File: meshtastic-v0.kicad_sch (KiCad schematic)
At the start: 0 parts

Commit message: Connect VSYS/3V3 sheet pins, sync R22, document remaining ERC state
Schematic/PCB edits: wire up the dangling VSYS and 3V3 hierarchical
sheet pins on the root sheet, and re-sync the board so R22 reads 1k
on both sides.

ERC 8 -> 6 errors; schematic parity 3 -> 2 issues; DRC still 0
violations and 0 unconnected pads.

README: explain each of the 6 remaining ERC errors (all PWR_FLAG /
no-connect annotations or the intentional JP3/JP4 jumper routing,
none of them wiring defects), and add an assembly note that JP3/JP4
ship unbridged and must be bridged for the display to receive power.

Co-Authored-By: Claude Opus 5 <noreply@anthropic.com>
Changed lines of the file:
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@@
+	(wire
+		(pts
+			(xy 191.77 81.28) (xy 191.77 69.85)
+		)
+		(stroke
+			(width 0)
+			(type default)
+		)
+	)
 	(wire
 		(pts
@@
 	(wire
 		(pts
+			(xy 186.69 69.85) (xy 186.69 78.74)
+		)
+		(stroke
+			(width 0)
+			(type default)
+		)
+	)
+	(wire
+		(pts
 			(xy 269.24 177.8) (xy 269.24 127)
 		)
@@
 	(wire
 		(pts
+			(xy 184.15 81.28) (xy 191.77 81.28)
+		)
+		(stroke
+			(width 0)
+			(type default)
+		)
+	)
+	(wire
+		(pts
 			(xy 189.23 220.98) (xy 189.23 205.74)
 		)
@@
 	(wire
 		(pts
+			(xy 186.69 78.74) (xy 184.15 78.74)
+		)
+		(stroke
+			(width 0)
+			(type default)
+		)
+	)
+	(wire
+		(pts
 			(xy 184.15 205.74) (xy 189.23 205.74)
 		)
@@
 		)
 	)
+	(symbol
+		(lib_id "power:+3V3")
+		(at 191.77 69.85 0)
+		(unit 1)
+		(body_style 1)
+		(exclude_from_sim no)
+		(in_bom yes)
+		(on_board yes)
+		(in_pos_files yes)
+		(dnp no)
+		(fields_autoplaced yes)
+		(property "Reference" "#PWR065"
+			(at 191.77 73.66 0)
+			(hide yes)
+			(show_name no)
+			(do_not_autoplace no)
+			(effects
+				(font
+					(size 1.27 1.27)
+				)
+			)
+		)
+		(property "Value" "+3V3"
+			(at 191.77 64.77 0)
+			(show_name no)
+			(do_not_autoplace no)
+			(effects
+				(font
+					(size 1.27 1.27)
+				)
+			)
+		)
+		(property "Footprint" ""
+			(at 191.77 69.85 0)
+			(hide yes)
+			(show_name no)
+			(do_not_autoplace no)
+			(effects
+				(font
+					(size 1.27 1.27)
+				)
+			)
+		)
+		(property "Datasheet" ""
+			(at 191.77 69.85 0)
+			(hide yes)
+			(show_name no)
+			(do_not_autoplace no)
+			(effects
+				(font
+					(size 1.27 1.27)
+				)
+			)
+		)
+		(property "Description" "Power symbol creates a global label with name \"+3V3\""
+			(at 191.77 69.85 0)
+			(hide yes)
+			(show_name no)
+			(do_not_autoplace no)
+			(effects
+				(font
+					(size 1.27 1.27)
+				)
+			)
+		)
+		(pin "1"
+		)
+		(instances
+			(project "meshtastic-v0"
+				(path "/e4d6fcd6-7415-4955-88fd-f0e430797514"
+					(reference "#PWR065")
+					(unit 1)
+				)
+			)
+		)
+	)
+	(symbol
+		(lib_id "power:VSS")
+		(at 186.69 69.85 0)
+		(unit 1)
+		(body_style 1)
+		(exclude_from_sim no)
+		(in_bom yes)
+		(on_board yes)
+		(in_pos_files yes)
+		(dnp no)
+		(fields_autoplaced yes)
+		(property "Reference" "#PWR012"
+			(at 186.69 73.66 0)
+			(hide yes)
+			(show_name no)
+			(do_not_autoplace no)
+			(effects
+				(font
+					(size 1.27 1.27)
+				)
+			)
+		)
+		(property "Value" "VSYS"
+			(at 186.69 64.77 0)
+			(show_name no)
+			(do_not_autoplace no)
+			(effects
+				(font
+					(size 1.27 1.27)
+				)
+			)
+		)
+		(property "Footprint" ""
+			(at 186.69 69.85 0)
+			(hide yes)
+			(show_name no)
+			(do_not_autoplace no)
+			(effects
+				(font
+					(size 1.27 1.27)
+				)
+			)
+		)
+		(property "Datasheet" ""
+			(at 186.69 69.85 0)
+			(hide yes)
+			(show_name no)
+			(do_not_autoplace no)
+			(effects
+				(font
+					(size 1.27 1.27)
+				)
+			)
+		)
+		(property "Description" "Power symbol creates a global label with name \"VSS\""
+			(at 186.69 69.85 0)
+			(hide yes)
+			(show_name no)
+			(do_not_autoplace no)
+			(effects
+				(font
+					(size 1.27 1.27)
+				)
+			)
+		)
+		(pin "1"
+		)
+		(instances
+			(project "meshtastic-v0"
+				(path "/e4d6fcd6-7415-4955-88fd-f0e430797514"
+					(reference "#PWR012")
+					(unit 1)
+				)
+			)
+		)
+	)

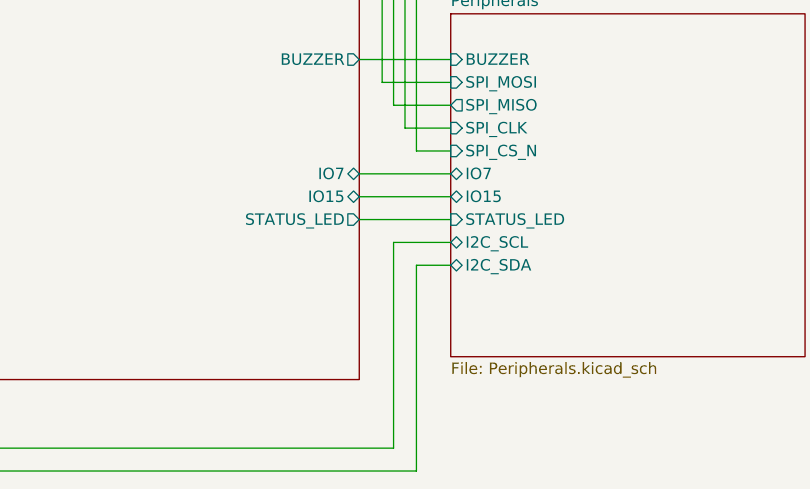
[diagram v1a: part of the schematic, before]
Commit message: Round board corners, re-annotate test points, rewrite README for GitHub
Board: 1.0 mm radius corners; outline now 71.00 x 46.00 mm.
Schematic: test points re-annotated to signal names (SDA1, SLC1,
CSN1, CLK1, MOSI1, MISO1, VS1, G1, G2, IO7, IO15, IO47, RST1, BOOT1).

README rewritten as a GitHub landing page: explains what the board is
for, adds Mermaid system-architecture and power-path diagrams, a
verified pin map traced from the netlist, board specs, and fab
instructions. Drops the ERC/DRC status and issue-tracking sections.

Co-Authored-By: Claude Opus 5 <noreply@anthropic.com>
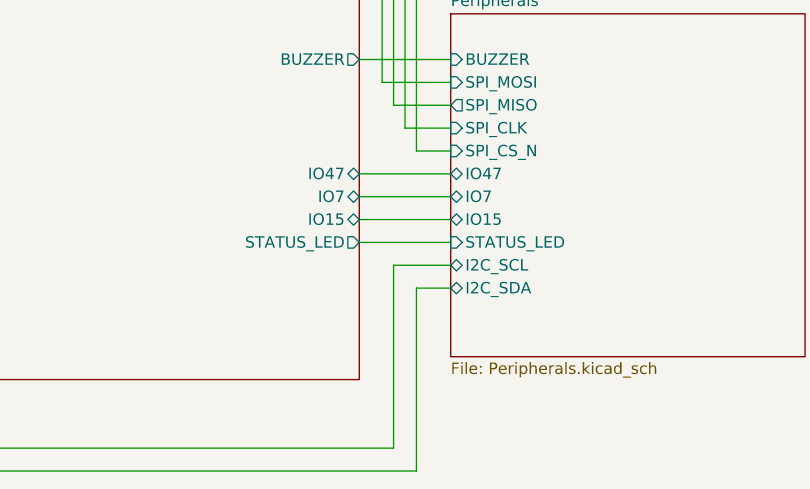
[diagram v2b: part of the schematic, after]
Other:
- sheet Microcontroller ports: added IO47; removed none
- sheet Peripherals ports: added IO47; removed none
